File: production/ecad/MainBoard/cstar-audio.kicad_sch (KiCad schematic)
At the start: 0 parts

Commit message: added connectors
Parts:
- added J1: 532610771, 532610771:MOLEX_532610771, symbol 532610771:532610771
- added J2: Conn_01x03_Pin, symbol Connector:Conn_01x03_Pin
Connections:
- new net +3V3: J1.3
- new net BICK: J1.7
- new net GND: J1.2
- new net LRCK: J1.5
- new net MCLK: J1.6
- new net SDTO: J1.4
- no-connect marks 0 -> 3
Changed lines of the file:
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@@
 (kicad_sch (version 20230121) (generator eeschema)
   (paper "A4")
+  (no_connect (at 138.43 90.17))
+  (no_connect (at 138.43 113.03))
+  (no_connect (at 138.43 110.49))
+  (wire (pts (xy 138.43 92.71) (xy 134.62 92.71))
+    (stroke (width 0) (type default))
+  )
+  (wire (pts (xy 134.62 92.71) (xy 134.62 85.09))
+    (stroke (width 0) (type default))
+  )
+  (wire (pts (xy 129.54 95.25) (xy 138.43 95.25))
+    (stroke (width 0) (type default))
+  )
+  (wire (pts (xy 134.62 85.09) (xy 129.54 85.09))
+    (stroke (width 0) (type default))
+  )
+  (hierarchical_label "BICK" (shape input) (at 138.43 105.41 180) (fields_autoplaced)
+    (effects (font (size 1.27 1.27)) (justify right))
+  )
+  (hierarchical_label "MCLK" (shape input) (at 138.43 102.87 180) (fields_autoplaced)
+    (effects (font (size 1.27 1.27)) (justify right))
+  )
+  (hierarchical_label "SDTO" (shape input) (at 138.43 97.79 180) (fields_autoplaced)
+    (effects (font (size 1.27 1.27)) (justify right))
+  )
+  (hierarchical_label "LRCK" (shape input) (at 138.43 100.33 180) (fields_autoplaced)
+    (effects (font (size 1.27 1.27)) (justify right))
+  )
+  (symbol (lib_id "power:+3V3") (at 129.54 95.25 0) (unit 1)
+    (in_bom yes) (on_board yes) (dnp no)
+    (property "Reference" "#PWR02" (at 129.54 99.06 0)
+      (effects (font (size 1.27 1.27)) hide)
+    )
+    (property "Value" "+3V3" (at 129.54 91.44 0)
+      (effects (font (size 1.27 1.27)))
+    )
+    (property "Footprint" "" (at 129.54 95.25 0)
+      (effects (font (size 1.27 1.27)) hide)
+    )
+    (property "Datasheet" "" (at 129.54 95.25 0)
+      (effects (font (size 1.27 1.27)) hide)
+    )
+    (pin "1")
+    (instances
+      (project "cstar-audio"
+        (path "/16a488a1-12e9-4eb7-bbd0-d500eeb9c89a"
+          (reference "#PWR02") (unit 1)
+        )
+      )
+      (project "MicBoard"
+        (path "/35817364-8fba-4697-86bd-839867f6fab6"
+          (reference "#PWR010") (unit 1)
+        )
+      )
+    )
+  )
+  (symbol (lib_id "Connector:Conn_01x03_Pin") (at 147.32 71.12 0) (unit 1)
+    (in_bom yes) (on_board yes) (dnp no) (fields_autoplaced)
+    (property "Reference" "J2" (at 147.955 63.5 0)
+      (effects (font (size 1.27 1.27)))
+    )
+    (property "Value" "Conn_01x03_Pin" (at 147.955 66.04 0)
+      (effects (font (size 1.27 1.27)))
+    )
+    (property "Footprint" "" (at 147.32 71.12 0)
+      (effects (font (size 1.27 1.27)) hide)
+    )
+    (property "Datasheet" "~" (at 147.32 71.12 0)
+      (effects (font (size 1.27 1.27)) hide)
+    )
+    (pin "1")
+    (pin "2")
+    (pin "3")
+    (instances
+      (project "cstar-audio"
+        (path "/16a488a1-12e9-4eb7-bbd0-d500eeb9c89a"
+          (reference "J2") (unit 1)
+        )
+      )
+    )
+  )
+  (symbol (lib_id "power:GND") (at 129.54 85.09 0) (unit 1)
+    (in_bom yes) (on_board yes) (dnp no)
+    (property "Reference" "#PWR01" (at 129.54 91.44 0)
+      (effects (font (size 1.27 1.27)) hide)
+    )
+    (property "Value" "GND" (at 129.54 88.9 0)
+      (effects (font (size 1.27 1.27)))
+    )
+    (property "Footprint" "" (at 129.54 85.09 0)
+      (effects (font (size 1.27 1.27)) hide)
+    )
+    (property "Datasheet" "" (at 129.54 85.09 0)
+      (effects (font (size 1.27 1.27)) hide)
+    )
+    (pin "1")
+    (instances
+      (project "cstar-audio"
+        (path "/16a488a1-12e9-4eb7-bbd0-d500eeb9c89a"
+          (reference "#PWR01") (unit 1)
+        )
+      )
+      (project "MicBoard"
+        (path "/35817364-8fba-4697-86bd-839867f6fab6"
+          (reference "#PWR011") (unit 1)
+        )
+      )
+    )
+  )
+  (symbol (lib_id "532610771:532610771") (at 151.13 100.33 0) (unit 1)
+    (in_bom yes) (on_board yes) (dnp no) (fields_autoplaced)
+    (property "Reference" "J1" (at 160.02 100.33 0)
+      (effects (font (size 1.27 1.27)) (justify left))
+    )
+    (property "Value" "532610771" (at 160.02 102.87 0)
+      (effects (font (size 1.27 1.27)) (justify left))
+    )
+    (property "Footprint" "532610771:MOLEX_532610771" (at 151.13 100.33 0)
+      (effects (font (size 1.27 1.27)) (justify bottom) hide)
+    )
+    (property "Datasheet" "" (at 151.13 100.33 0)
+      (effects (font (size 1.27 1.27)) hide)
+    )
+    (property "DigiKey_Part_Number" "WM7625TR-ND" (at 151.13 100.33 0)
+      (effects (font (size 1.27 1.27)) (justify bottom) hide)
+    )
+    (property "MF" "Molex" (at 151.13 100.33 0)
+      (effects (font (size 1.27 1.27)) (justify bottom) hide)
+    )
+    (property "MAXIMUM_PACKAGE_HEIGHT" "3.4 mm" (at 151.13 100.33 0)
+      (effects (font (size 1.27 1.27)) (justify bottom) hide)
+    )
+    (property "Package" "None" (at 151.13 100.33 0)
+      (effects (font (size 1.27 1.27)) (justify bottom) hide)
+    )
+    (property "Check_prices" "https://www.snapeda.com/parts/0532610771/Molex/view-part/?ref=eda" (at 151.13 100.33 0)
+      (effects (font (size 1.27 1.27)) (justify bottom) hide)
+    )
+    (property "STANDARD" "Manufacturer Recommendations" (at 151.13 100.33 0)
+      (effects (font (size 1.27 1.27)) (justify bottom) hide)
+    )
+    (property "PARTREV" "J" (at 151.13 100.33 0)
+      (effects (font (size 1.27 1.27)) (justify bottom) hide)
+    )
+    (property "SnapEDA_Link" "https://www.snapeda.com/parts/0532610771/Molex/view-part/?ref=snap" (at 151.13 100.33 0)
+      (effects (font (size 1.27 1.27)) (justify bottom) hide)
+    )
+    (property "MP" "0532610771" (at 151.13 100.33 0)
+      (effects (font (size 1.27 1.27)) (justify bottom) hide)
+    )
+    (property "Purchase-URL" "https://www.snapeda.com/api/url_track_click_mouser/?unipart_id=577144&manufacturer=Molex&part_name=0532610771&search_term=None" (at 151.13 100.33 0)
+      (effects (font (size 1.27 1.27)) (justify bottom) hide)
+    )
+    (property "Description" "\nPicoblade Connector, 7 Circuit Single Row, Right Angle Surface Mount SMT PCB\n" (at 151.13 100.33 0)
+      (effects (font (size 1.27 1.27)) (justify bottom) hide)
+    )
+    (property "MANUFACTURER" "Molex" (at 151.13 100.33 0)
+      (effects (font (size 1.27 1.27)) (justify bottom) hide)
+    )
+    (pin "1")
+    (pin "2")
+    (pin "3")
+    (pin "4")
+    (pin "5")
+    (pin "6")
+    (pin "7")
+    (pin "S1")
+    (pin "S2")
+    (instances
+      (project "cstar-audio"
+        (path "/16a488a1-12e9-4eb7-bbd0-d500eeb9c89a"
+          (reference "J1") (unit 1)
+        )
+      )
+      (project "cstar-lidar"
+        (path "/f4254b98-3297-4812-862b-6470cd23e6be"
+          (reference "J1") (unit 1)
+        )
+      )
+    )
+  )
+  (sheet_instances
+    (path "/" (page "1"))
+  )
 )

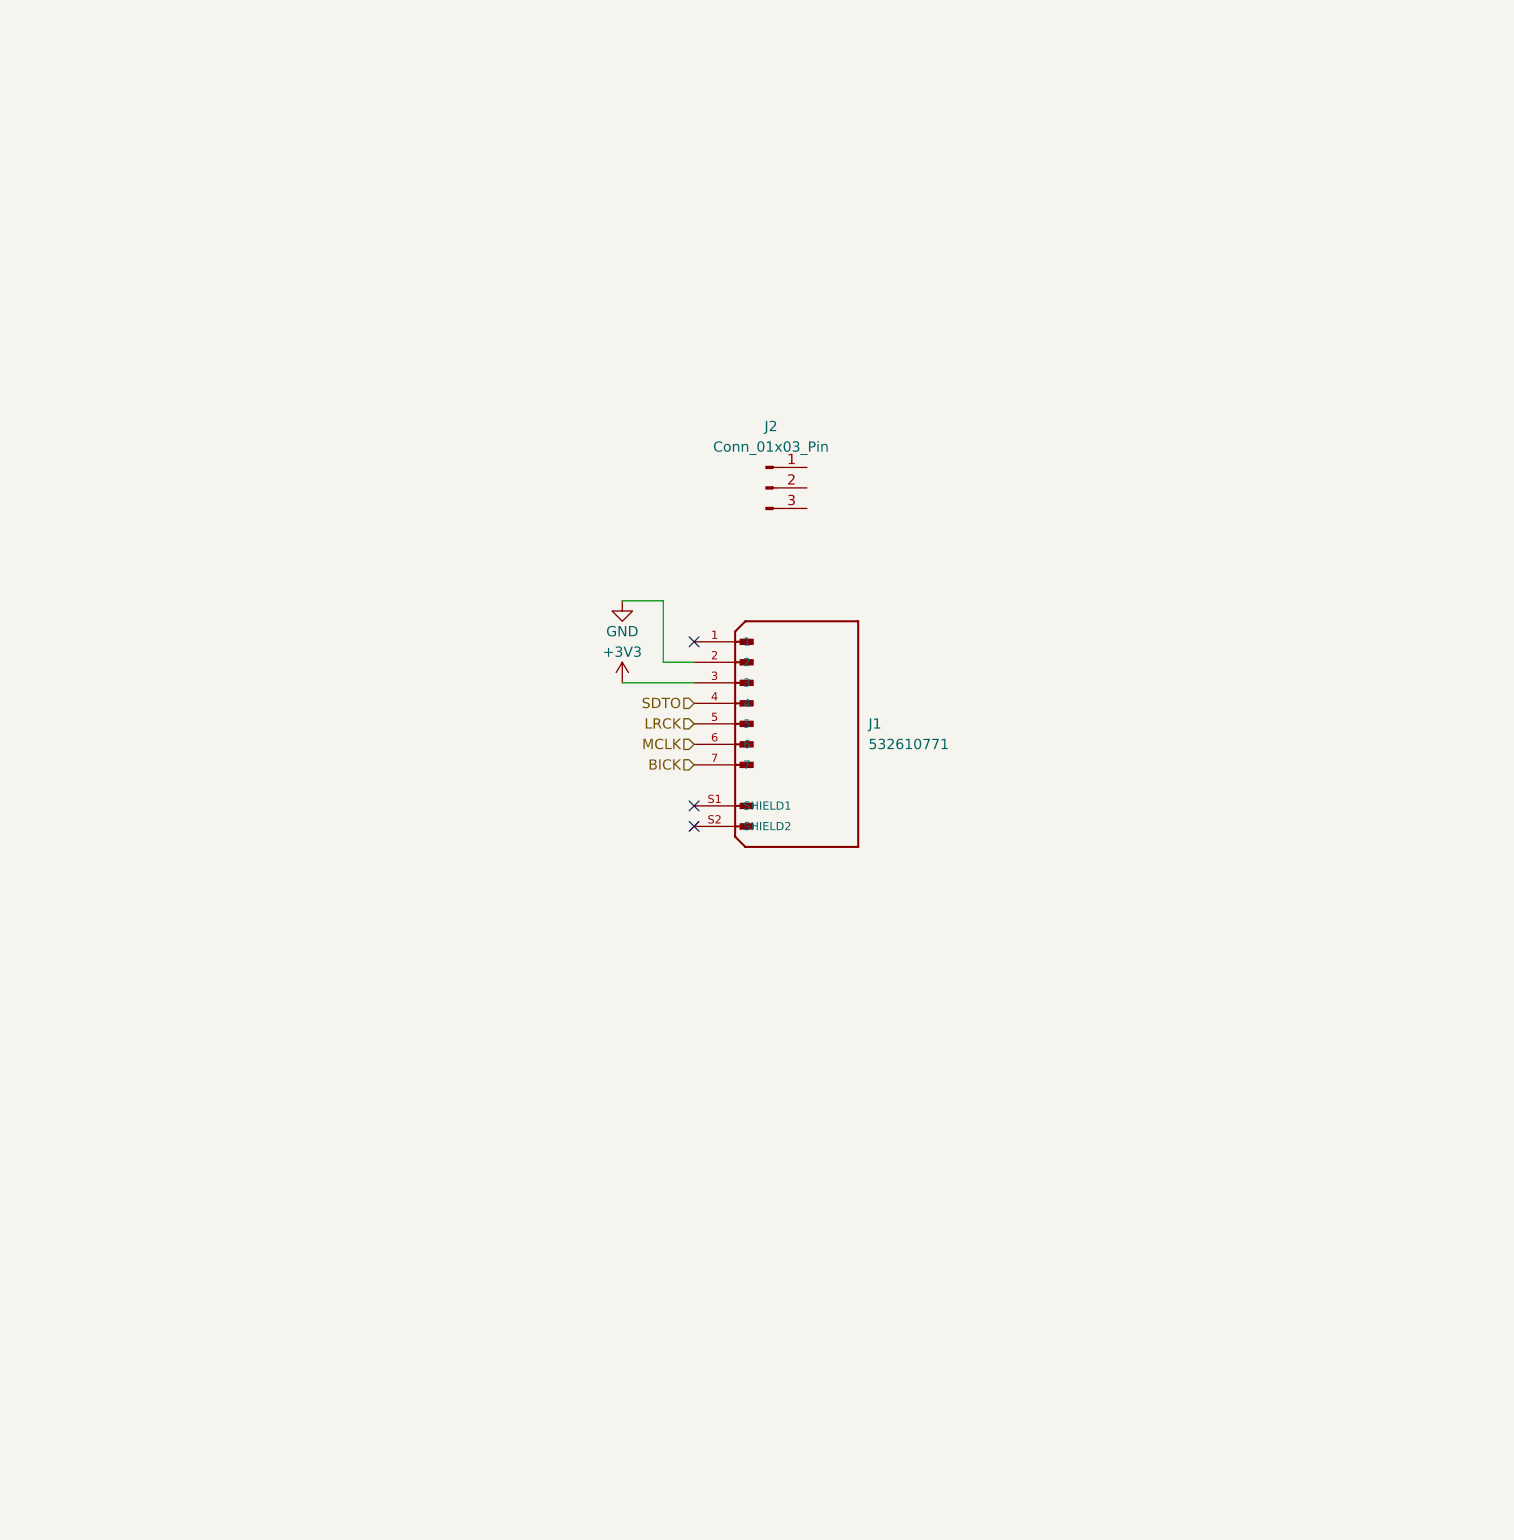
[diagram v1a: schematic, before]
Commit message: add ground shields and extra connector
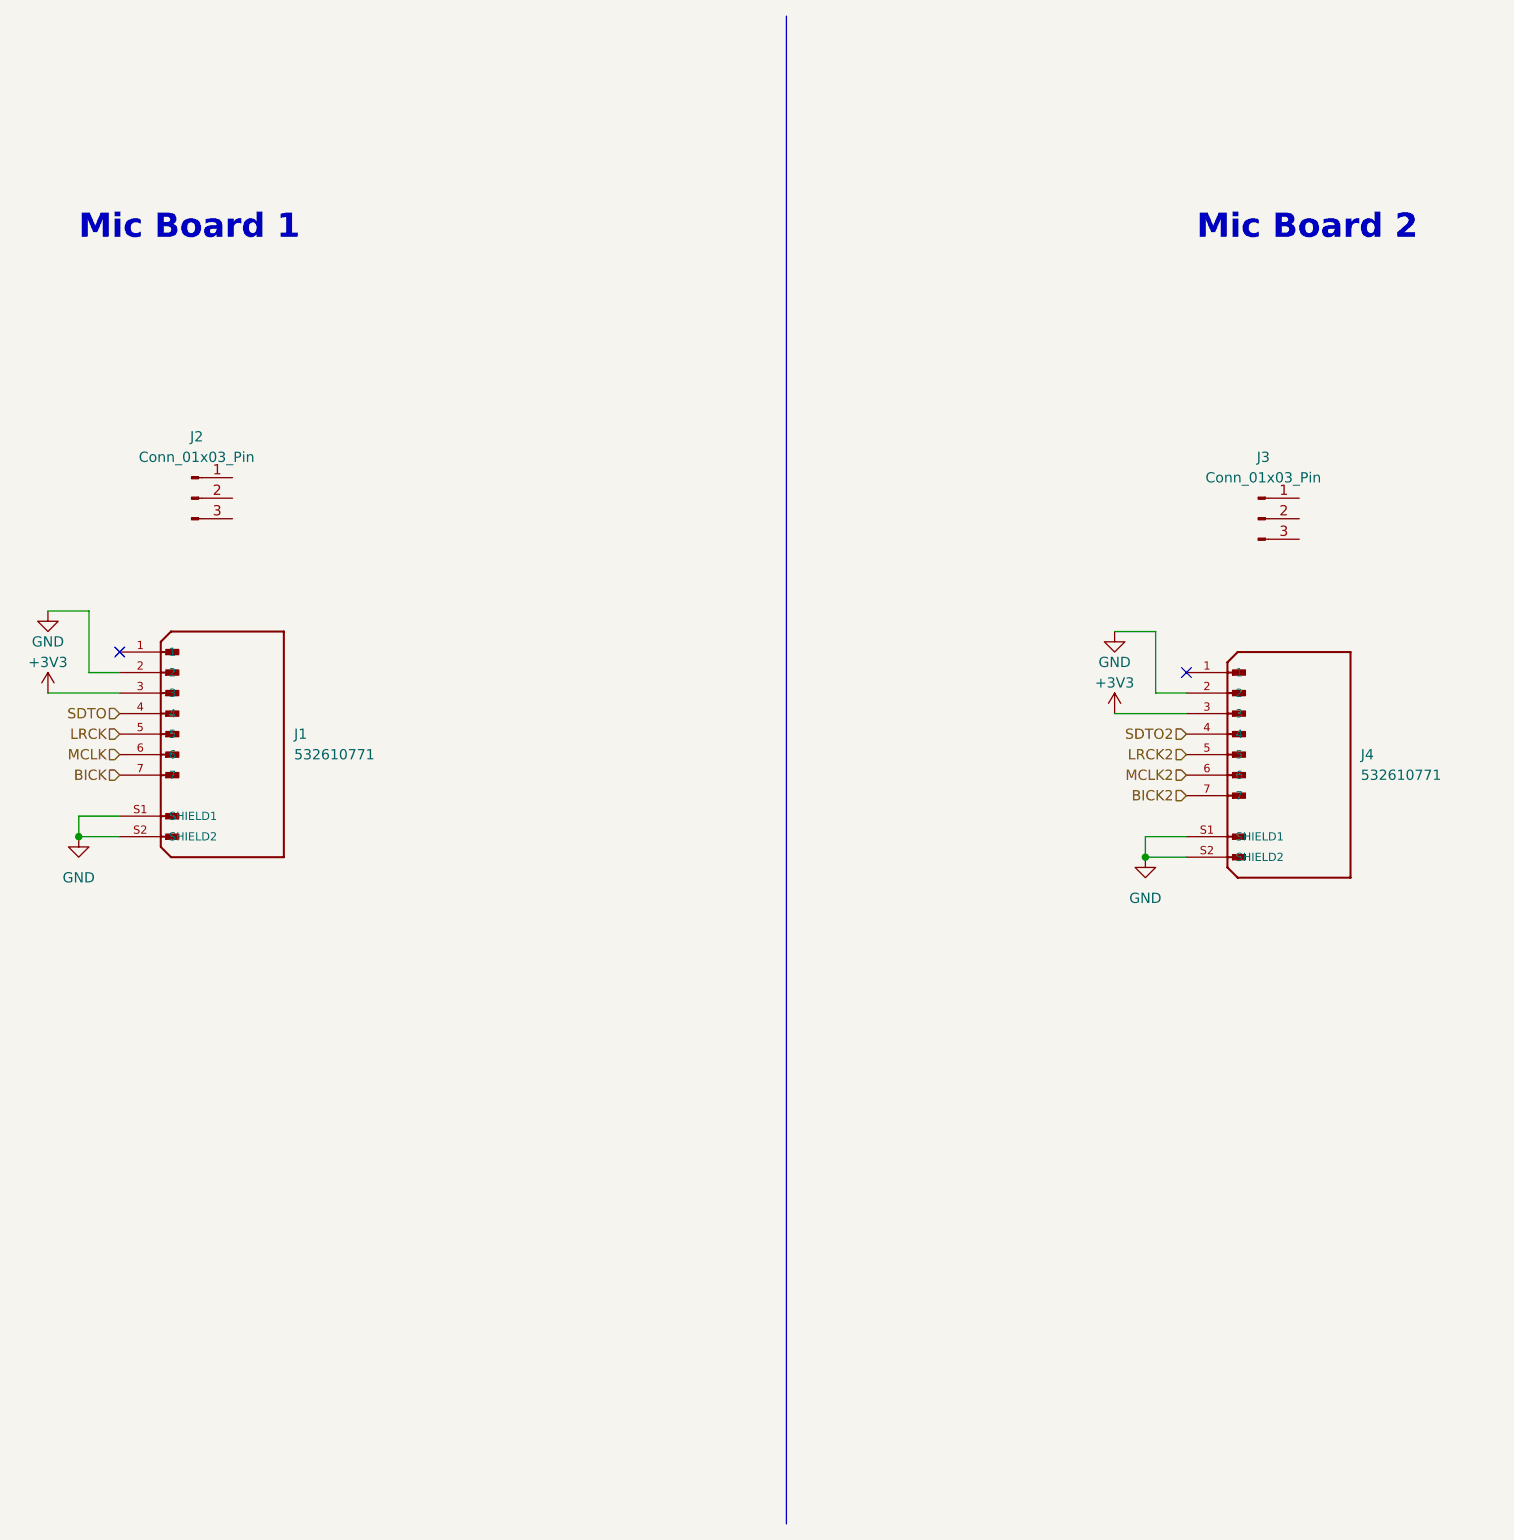
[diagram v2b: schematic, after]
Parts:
- added J3: Conn_01x03_Pin, symbol Connector:Conn_01x03_Pin
- added J4: 532610771, 532610771:MOLEX_532610771, symbol 532610771:532610771
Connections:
- net +3V3: now also J4.3
- net GND: now also J1.S1 (SHIELD1), J1.S2 (SHIELD2), J4.2, J4.S1 (SHIELD1), J4.S2 (SHIELD2)
- new net BICK2: J4.7
- new net LRCK2: J4.5
- new net MCLK2: J4.6
- new net SDTO2: J4.4
- no-connect marks 3 -> 2
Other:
- note added: "Mic Board 1"
- note added: "Mic Board 2"
- moved on the sheet: J1, J2

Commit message: change to global net
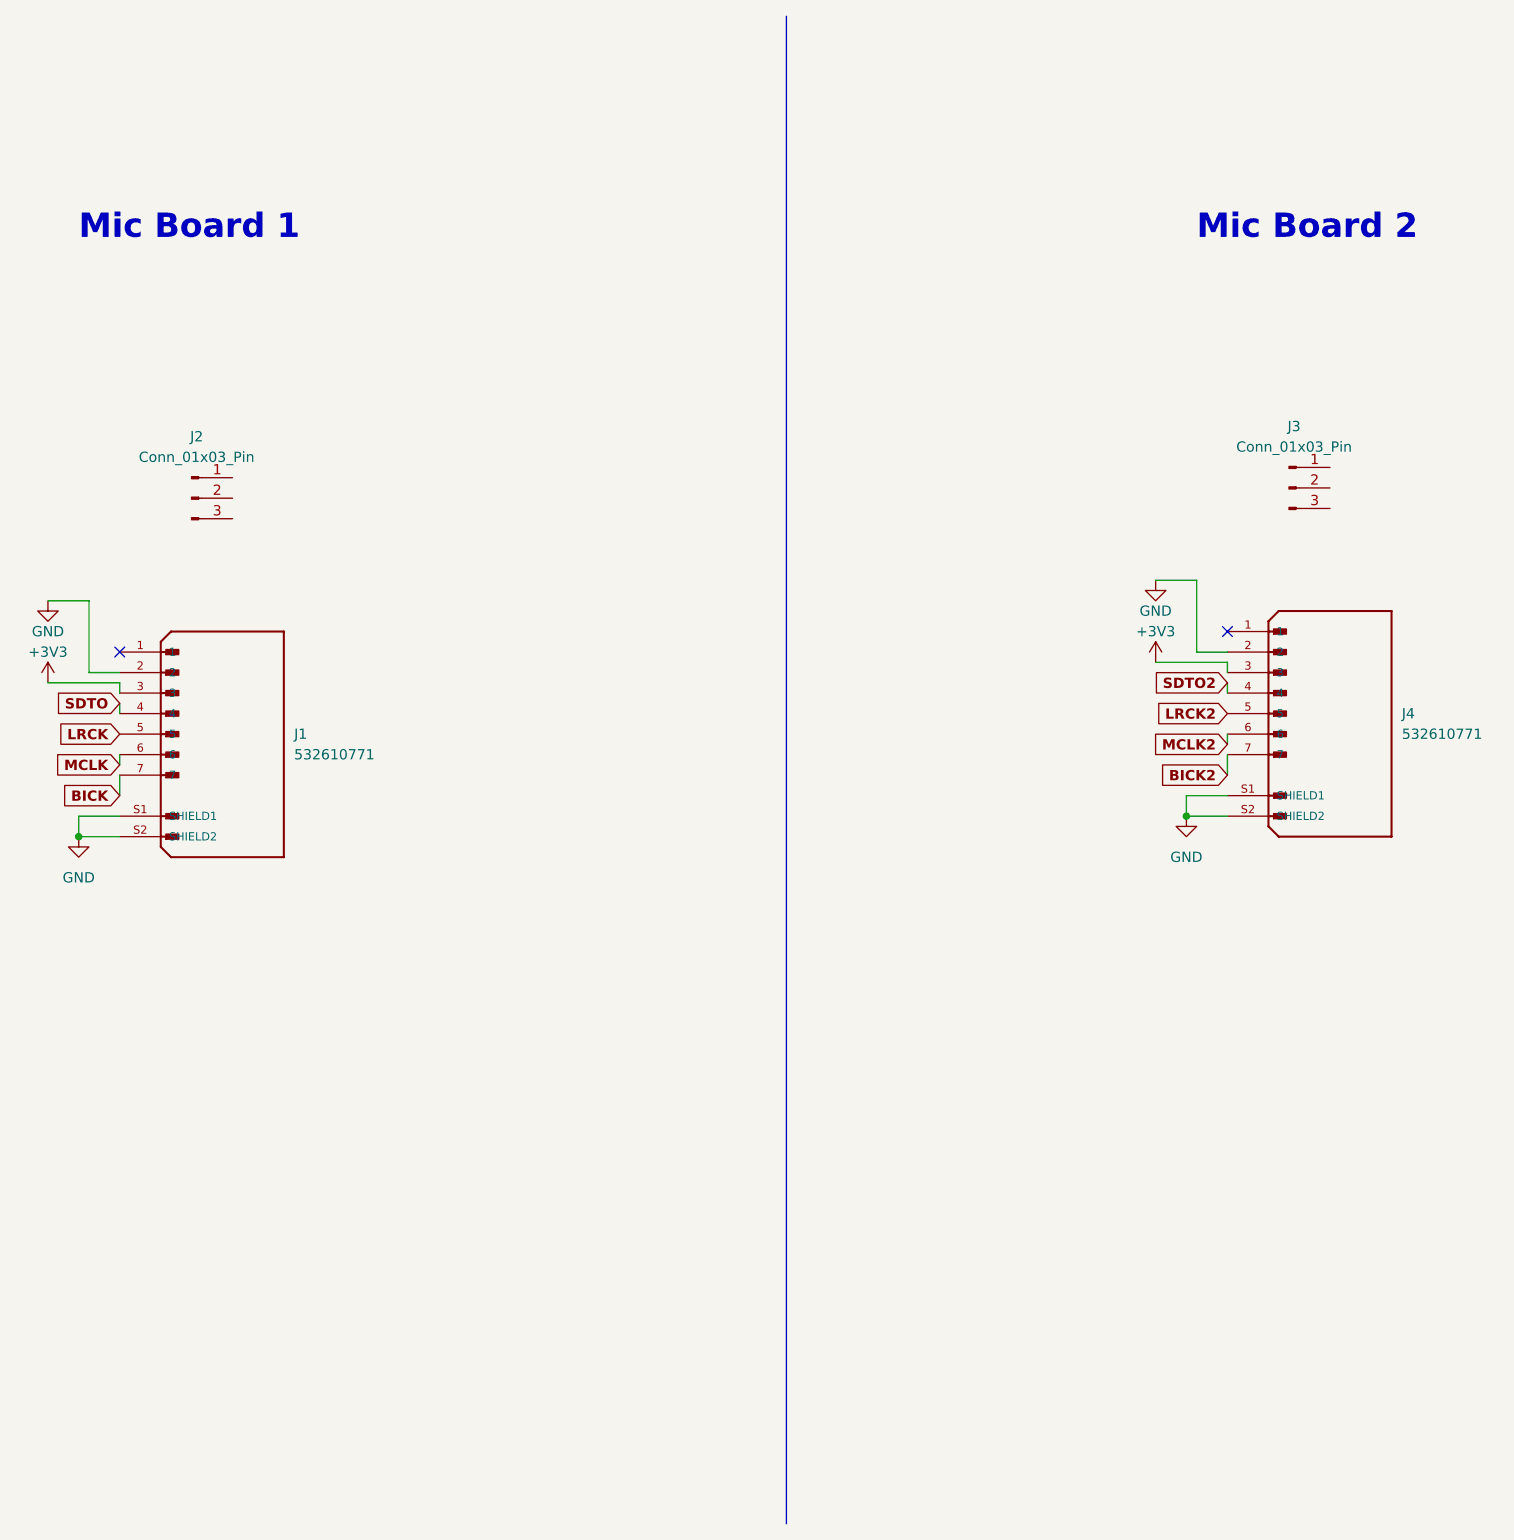
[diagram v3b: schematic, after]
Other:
- moved on the sheet: J3

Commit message: mic footprints (0805 connector pins)
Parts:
- J2, J3: footprint (none) -> Connector_Phoenix_SPT:PhoenixContact_SPT_1.5_9-H-3.5_1x09_P3.5mm_Horizontal
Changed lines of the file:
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@@
       (effects (font (size 1.27 1.27)))
     )
-    (property "Footprint" "" (at 212.09 71.12 0)
+    (property "Footprint" "Connector_Phoenix_SPT:PhoenixContact_SPT_1.5_9-H-3.5_1x09_P3.5mm_Horizontal" (at 212.09 71.12 0)
       (effects (font (size 1.27 1.27)) hide)
     )
@@
       (effects (font (size 1.27 1.27)))
     )
-    (property "Footprint" "" (at 76.2 72.39 0)
+    (property "Footprint" "Connector_Phoenix_SPT:PhoenixContact_SPT_1.5_9-H-3.5_1x09_P3.5mm_Horizontal" (at 76.2 72.39 0)
       (effects (font (size 1.27 1.27)) hide)
     )
